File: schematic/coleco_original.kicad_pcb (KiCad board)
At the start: 2 copper layers, 168.4 x 318 mm, 220 parts, among them J0 Conn_01x04, J1 Cartridge Port, J2 Expansion Port, J4A1 Conn_01x08, J4B1 Conn_01x08, J5 DB9_Male, J6 DB9_Male, Q2 2N3906, Q3 2N3906, Q4 2N3904, Q5 2N3904, Q6 2N3906, U1 Z80CPU, U10 MK4116P, U11 MK4116P, U12 MK4116P, U13 MK4116P, U14 MK4116P, U15 MK4116P, U16 MK4116P, U17 MK4116P, U18 74LS541, U19 74LS541, U2 27C256, U20 SN76489AN, U22 74LS04, U23 4066, U24 74LS00, U3 SCM2114AL, U4 SCM2114AL, U5 74LS138, U6 74LS138, U7 74LS05, U8 74LS74, U9 TMS9928A, Y1 7.159090Mhz

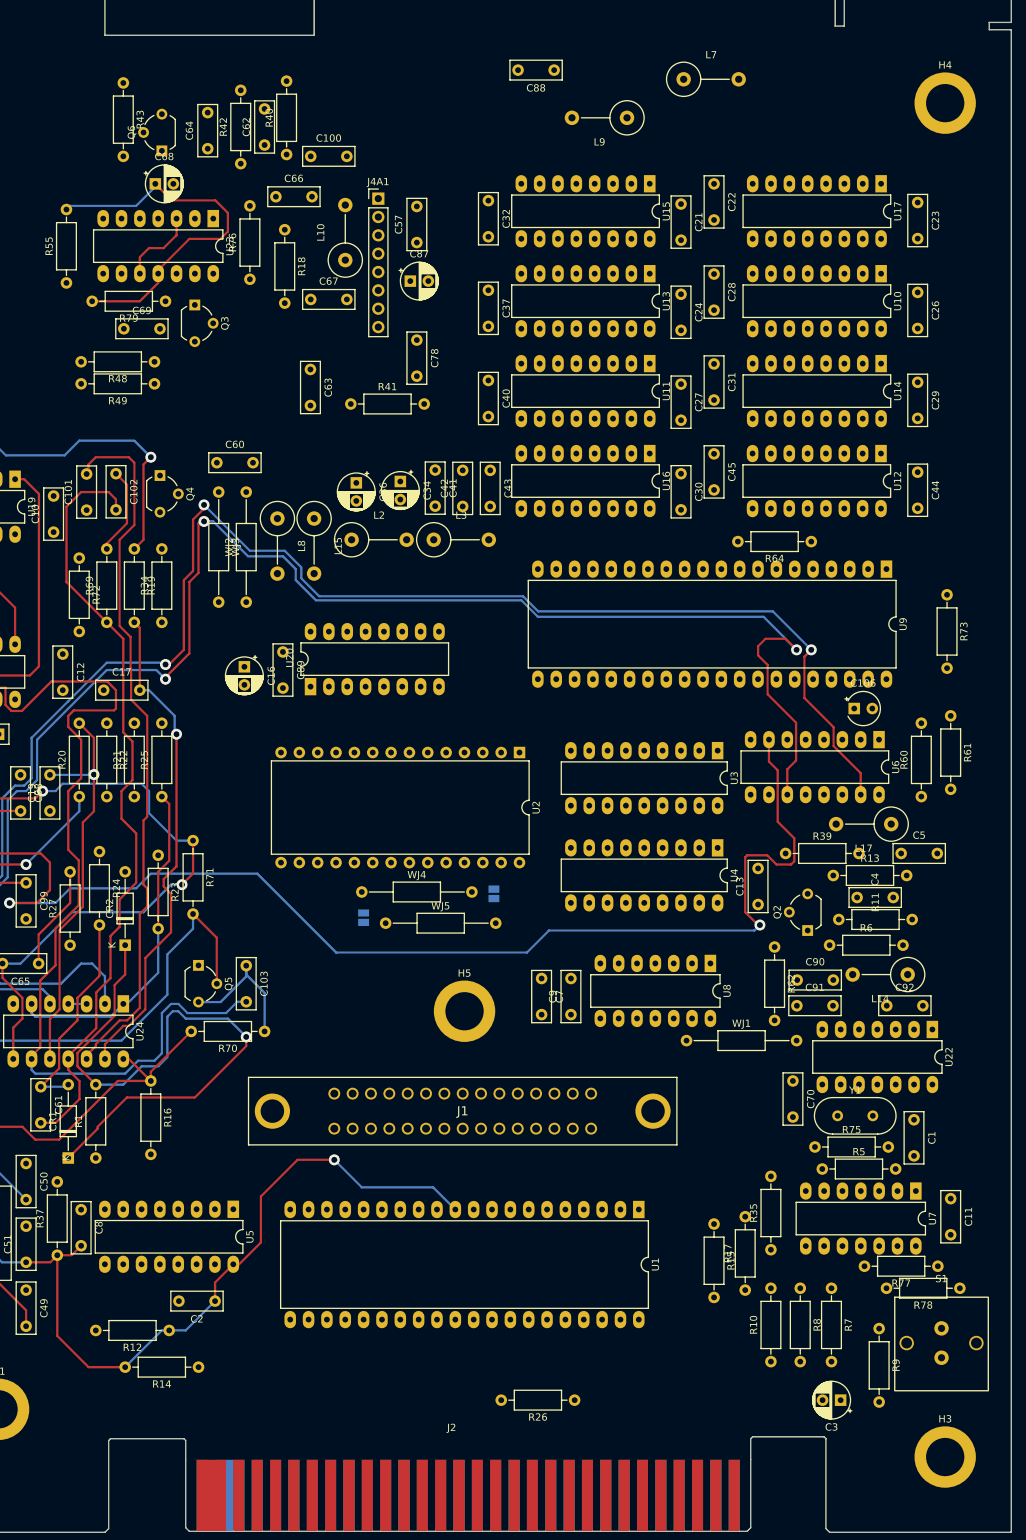
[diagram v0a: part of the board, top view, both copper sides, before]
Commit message: added addr decode and 4066 circuit
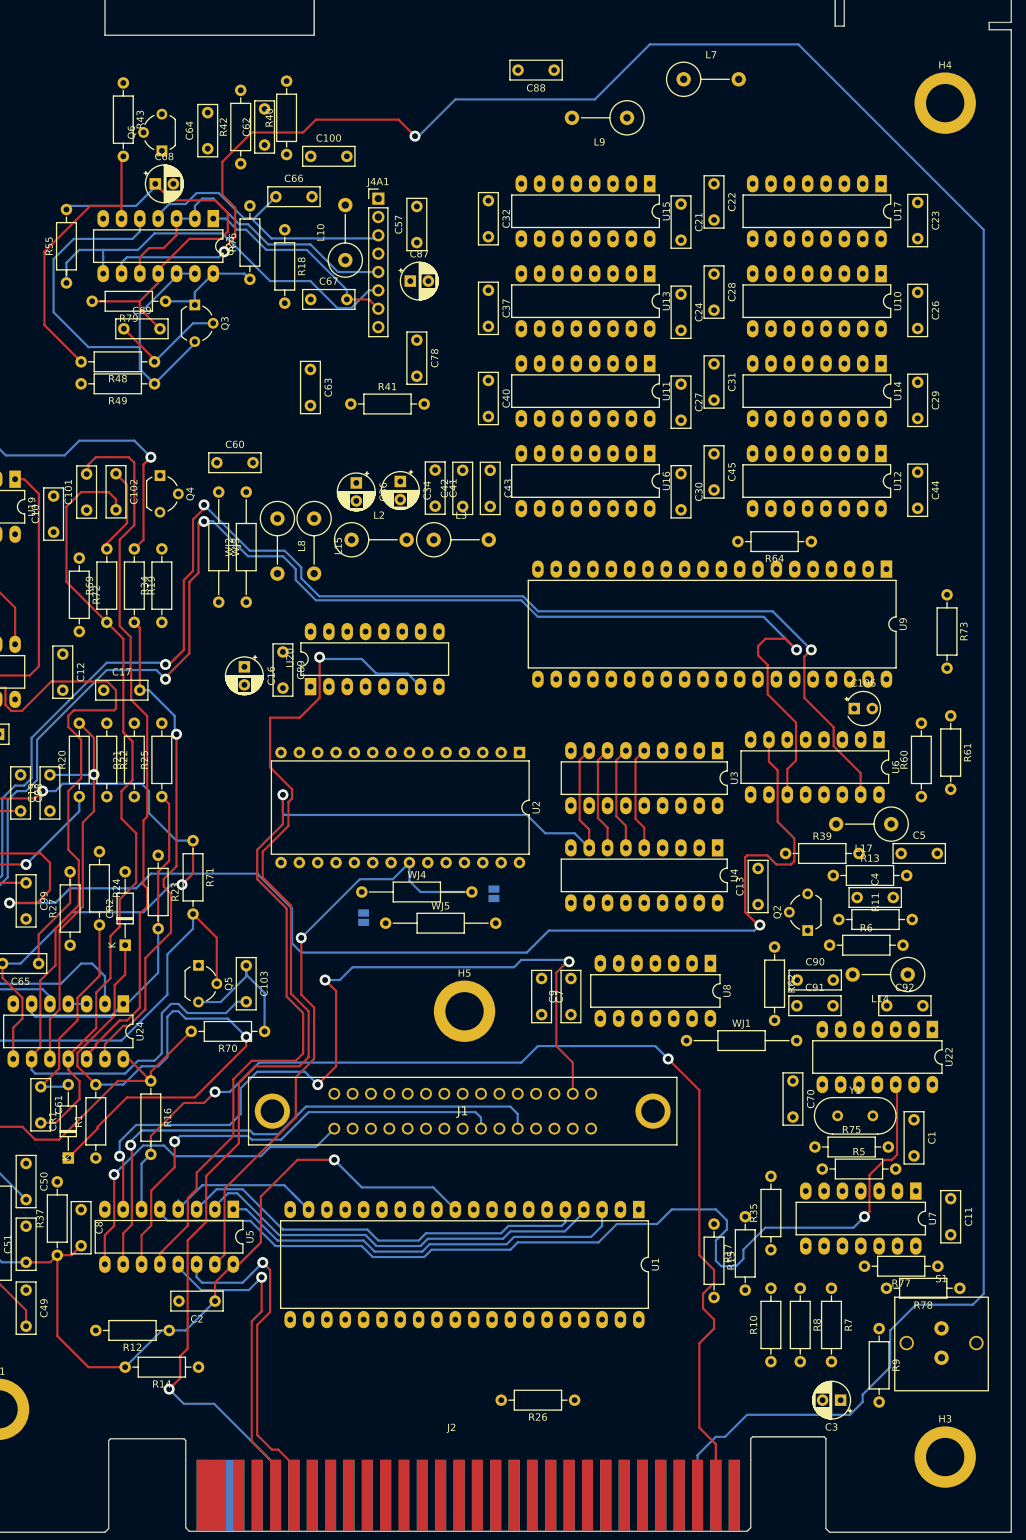
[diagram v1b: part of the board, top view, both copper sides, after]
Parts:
- J1: footprint TE_5530841-2:55308412 -> TE_5530841-2:55308412_coleco
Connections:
- J1 pad 2: /decoder_logic/~{CS_hE000} -> /decoder_logic/~{CS_hC000}
- J1 pad 27: /decoder_logic/~{CS_hC000} -> /decoder_logic/~{CS_hE000}
- Q3 pad 1: Net-(Q3-Pad1) -> VDDA
- R79 pad 1: Net-(Q3-Pad1) -> VDDA
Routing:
- net /io_ports/EXT_VIDEO: track 0.00 -> 360.2 mm, vias 0 -> 2
- net /io_ports/SND_OUT: track 0.00 -> 162.7 mm, vias 0 -> 2
- net /decoder_logic/AUX_DECODE_1: track 0.00 -> 154.3 mm, vias 0 -> 2
- net /decoder_logic/~{RAM_CS}: track 0.00 -> 142.4 mm, vias 0 -> 1
- net /clock_reset_misc_logic/RFSH: track 0.00 -> 136.4 mm, vias 0 -> 1
- net /decoder_logic/~{CS_hE000}: track 0.00 -> 115.2 mm, vias 0 -> 4
- net /decoder_logic/~{ROM_ENABLE}: track 0.00 -> 82.7 mm, vias 0 -> 1
- net /decoder_logic/~{CS_hA000}: track 0.00 -> 76.0 mm, vias 0 -> 1
- net Net-(Q3-Pad3): track 0.00 -> 65.5 mm
- net /decoder_logic/~{CS_h8000}: track 0.00 -> 65.3 mm, vias 0 -> 1
- net /cpu/A15: track 0.00 -> 58.0 mm
- net /cpu/A14: track 0.00 -> 57.6 mm
- net /cpu/A13: track 0.00 -> 57.2 mm
- net /rf_mod/sub_rf_mod/6: track 41.0 -> 97.8 mm
- net /decoder_logic/~{CS_h2000}: track 0.00 -> 48.5 mm, vias 0 -> 1
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
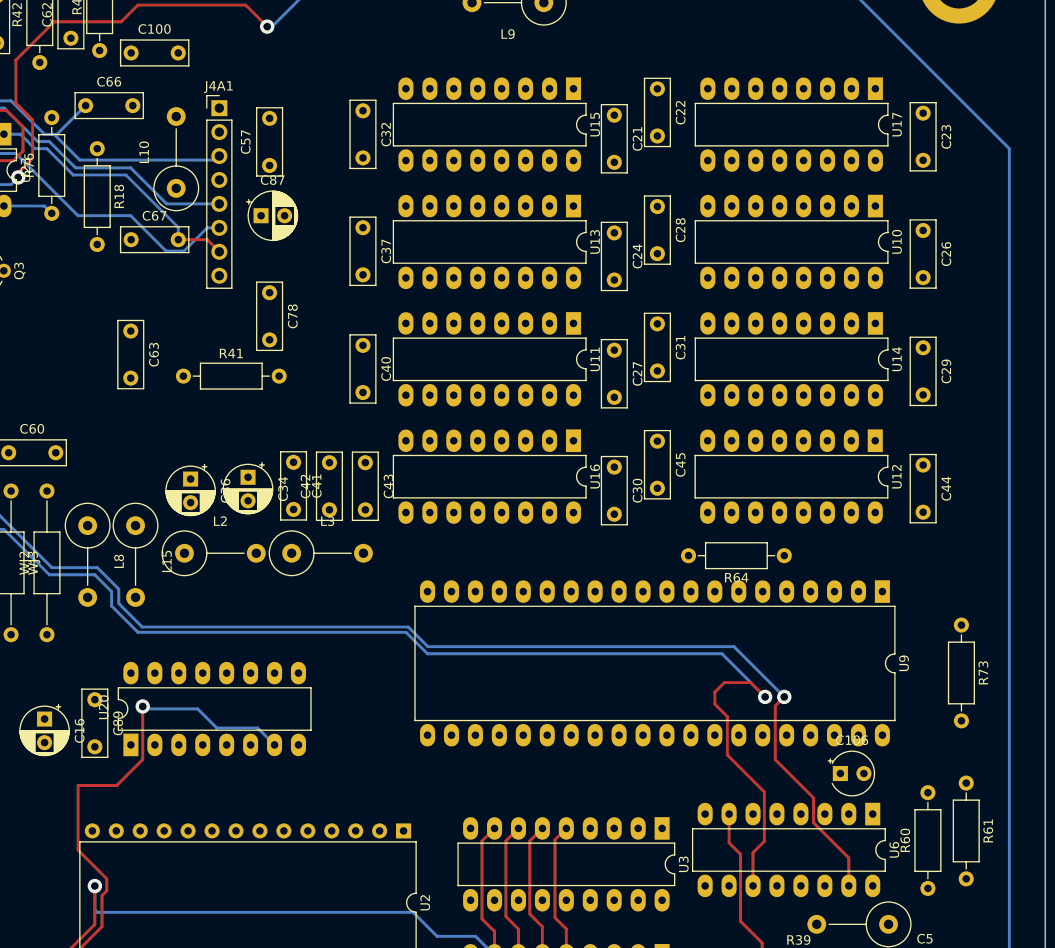
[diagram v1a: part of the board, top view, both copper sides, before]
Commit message: added video memory connections
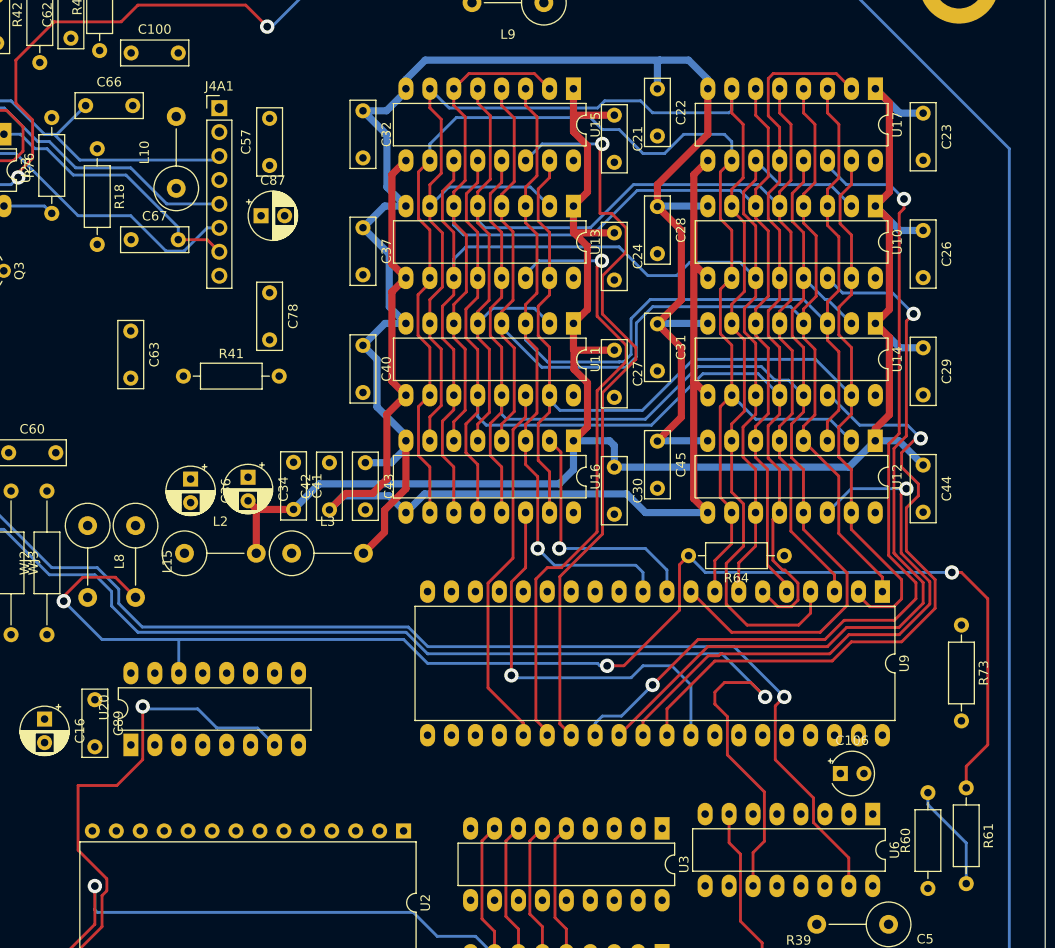
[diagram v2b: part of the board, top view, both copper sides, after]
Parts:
- moved R61 0.51 mm to (213.4, 129.4)
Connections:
- R64 pad 2: Net-(Q2-Pad3) -> /clock_reset_misc_logic/SND_CLK
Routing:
- net -5V: track 0.00 -> 201.0 mm
- net +12V: track 0.00 -> 171.1 mm
- net /video/AD6: track 0.00 -> 162.8 mm
- net /video/AD1: track 0.00 -> 157.0 mm
- net /video/AD4: track 0.00 -> 153.1 mm
- net Net-(U10-Pad3): track 0.00 -> 147.7 mm, vias 0 -> 1
- net /video/AD5: track 0.00 -> 147.1 mm
- net /video/AD7: track 0.00 -> 145.0 mm
- net /clock_reset_misc_logic/SND_CLK: track 0.00 -> 144.9 mm, vias 0 -> 3
- net /video/AD2: track 0.00 -> 144.2 mm
- net /video/AD3: track 0.00 -> 139.3 mm
- net Net-(U10-Pad4): track 0.00 -> 139.1 mm
- net Net-(U10-Pad15): track 0.00 -> 134.9 mm
- net +5V: track 168.3 -> 298.7 mm
- net Net-(U17-Pad14): track 0.00 -> 95.2 mm, vias 0 -> 2
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
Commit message: added traces to parts of the clock gen/reset ic's
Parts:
- moved R76 10.4 mm to (116.3, 58.1), turned to -90 degrees
- moved R75 10.2 mm to (204.7, 188.6), turned to 180 degrees
- moved Y1 4.48 mm to (202.2, 184.3), turned to 180 degrees
- moved C36 2.54 mm to (131.1, 99.2), turned to 90 degrees
- moved C92 1.52 mm to (203.0, 169.0)
- moved R64 0.51 mm to (194.1, 104.3)
- moved R77 0.25 mm to (211.6, 205.4)
- moved R78 0.25 mm to (214.6, 208.4)
- moved S1 0.25 mm to (212.1, 209.7)
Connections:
- C36 pad 1: GNDD -> +12V
- C36 pad 2: +12V -> GNDD
- Q3 pad 1: VDDA -> +12VL
- R76 pad 1: VDDA -> Net-(C68-Pad2)
- R76 pad 2: Net-(C68-Pad2) -> +12VL
- R79 pad 1: VDDA -> +12VL
- U23 pad 14: VDDA -> +12VL
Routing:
- net /clock_reset_misc_logic/~{WAIT}: track 0.00 -> 236.4 mm, vias 0 -> 3
- net /clock_reset_misc_logic/~{CTRL_READ_2}: track 0.00 -> 235.1 mm, vias 0 -> 2
- net /clock_reset_misc_logic/INT: track 85.3 -> 245.3 mm, vias 1 -> 4
- net /clock_reset_misc_logic/~{INT}: track 0.00 -> 127.7 mm, vias 0 -> 3
- net /cpu/A1: track 14.6 -> 138.7 mm, vias 0 -> 1
- net /clock_reset_misc_logic/~{RFSH}: track 0.00 -> 119.4 mm, vias 0 -> 1
- net /clock_reset_misc_logic/~{M1}: track 0.00 -> 108.8 mm, vias 0 -> 3
- net /clock_reset_misc_logic/~{RESET}: track 0.00 -> 93.0 mm
- net /clock_reset_misc_logic/EXP_RESET: track 0.00 -> 65.7 mm
- net +12VL: track 10.2 -> 75.0 mm, vias 0 -> 1
- net +5V: track 298.7 -> 362.1 mm
- net Net-(U7-Pad3): track 0.00 -> 60.7 mm, vias 0 -> 1
- net /clock_reset_misc_logic/VDP_CLK: track 0.00 -> 54.0 mm
- net Net-(C70-Pad1): track 0.00 -> 51.9 mm
- net VDDA: track 15.1 -> 55.6 mm, vias 0 -> 1
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
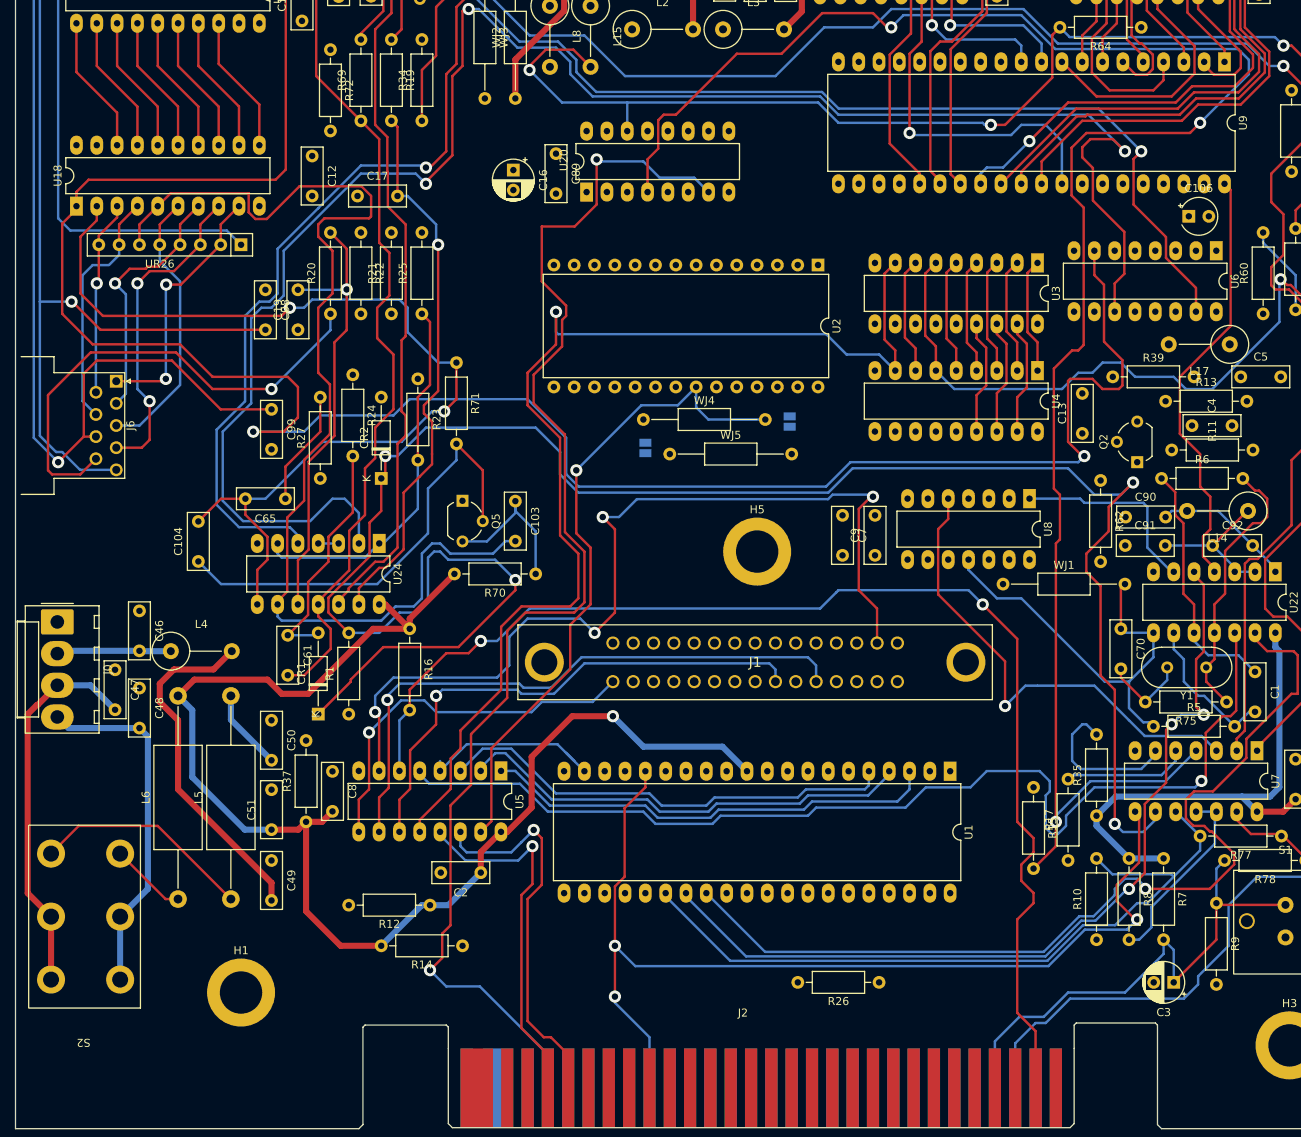
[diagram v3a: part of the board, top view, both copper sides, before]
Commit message: fixed a bug on the +5v line, added +5NF (no filter) net list names. Added traces to the ram, and inverter, and select ics.
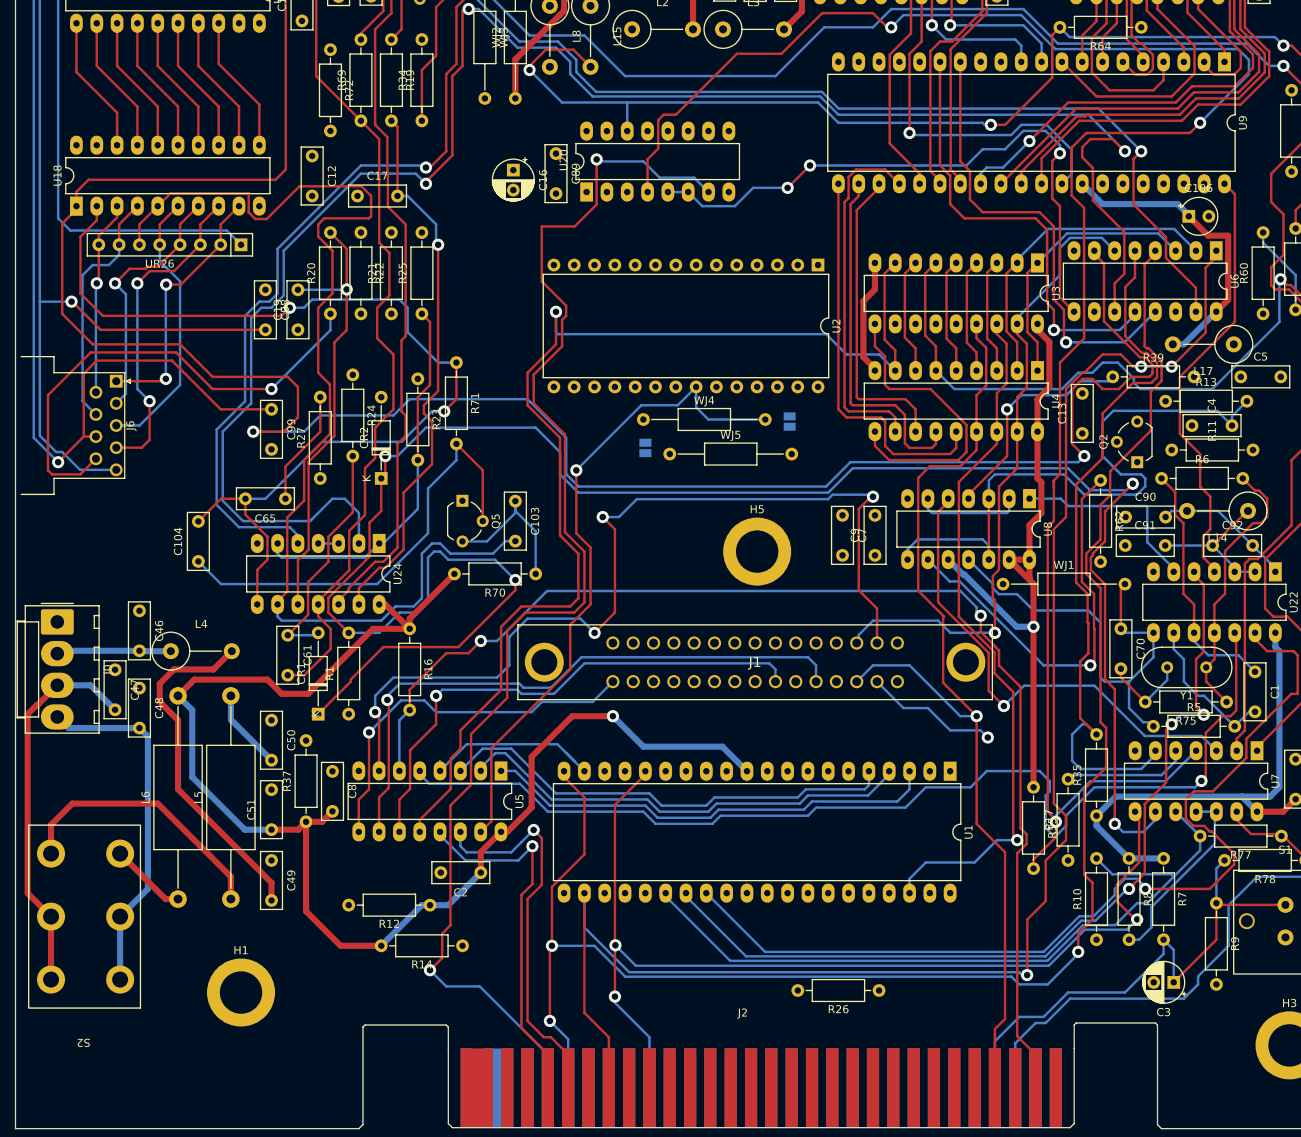
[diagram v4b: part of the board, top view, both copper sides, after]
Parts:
- moved R26 1.02 mm to (161.3, 224.7)
- moved L17 0.51 mm to (205.6, 143.9)
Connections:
- net Net-(L5-Pad1) renamed /psu/+12NF
- net Net-(L6-Pad1) renamed /psu/+5NF
- U6 pad 16: +5V -> +5VD
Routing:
- net /cpu/~{WR}: track 0.00 -> 234.8 mm, vias 0 -> 3
- net /cpu/~{IORQ}: track 0.00 -> 209.4 mm, vias 0 -> 3
- net /cpu/A9: track 14.5 -> 125.3 mm, vias 0 -> 1
- net /cpu/A8: track 14.5 -> 104.5 mm, vias 0 -> 2
- net +5V: track 362.1 -> 442.5 mm, vias 1 -> 2
- net Net-(C4-Pad2): track 0.00 -> 78.4 mm
- net /decoder_logic/~{SND_ENABLE}: track 0.00 -> 76.7 mm, vias 0 -> 3
- net /clock_reset_misc_logic/~{AUD_DECODE_2}: track 19.5 -> 89.9 mm
- net /cpu/A7: track 14.5 -> 80.2 mm, vias 0 -> 1
- net /decoder_logic/~{CSW}: track 0.00 -> 57.4 mm, vias 0 -> 1
- net /decoder_logic/~{CSR}: track 0.00 -> 55.9 mm, vias 0 -> 1
- net Net-(Q2-Pad3): track 11.3 -> 62.1 mm, vias 0 -> 1
- net /cpu/D4: track 17.3 -> 66.7 mm
- net /cpu/D7: track 17.3 -> 62.4 mm
- net /cpu/D5: track 17.3 -> 62.0 mm
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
